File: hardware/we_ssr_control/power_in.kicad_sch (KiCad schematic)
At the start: 10 parts, among them Q1 IRF4905PBF

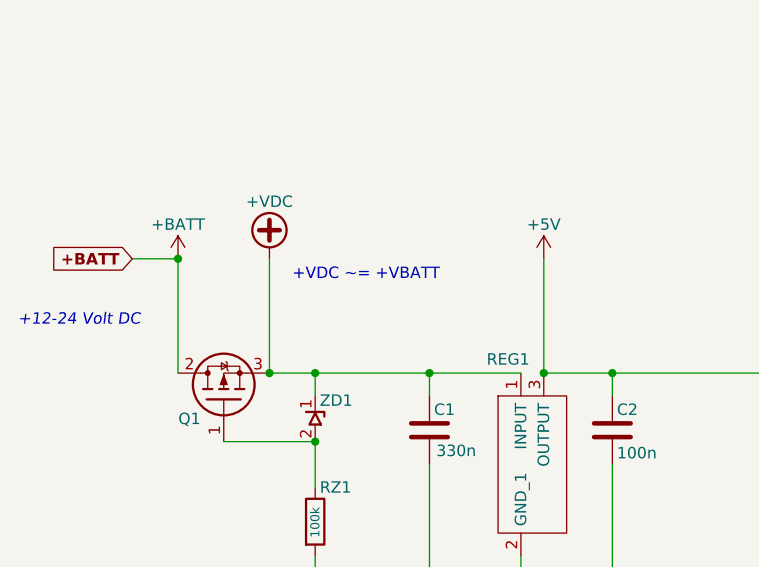
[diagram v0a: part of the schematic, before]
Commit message: Corrected footprint of RZ1 from 0805 to 0603
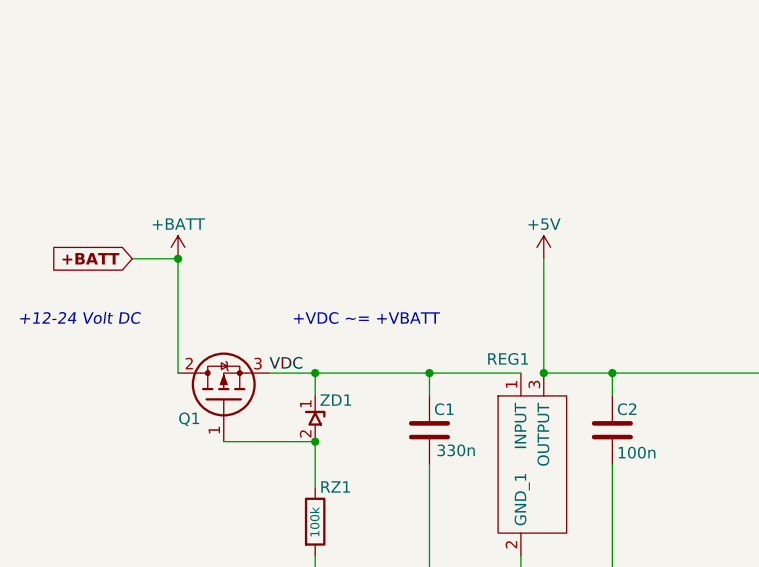
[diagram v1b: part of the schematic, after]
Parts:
- RZ1: footprint Resistor_SMD:R_0805_2012Metric -> Resistor_SMD:R_0603_1608Metric
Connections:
- net +VDC renamed VDC

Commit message: Merged all symbol, 3dmodel, and footprint changes
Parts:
- Q1: Manufacturer_Name (none) -> Infineon; Manufacturer_Part_Number (none) -> IRF4905PBF
